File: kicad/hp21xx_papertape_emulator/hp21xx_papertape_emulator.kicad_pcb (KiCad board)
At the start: 2 copper layers, 66.5 x 61.2 mm, 85 parts, among them J1 SWD, J2 SERIAL, J3 Micro_SD_Card_Det_Hirose_DM3AT, J5 Conn_02x13_Odd_Even, SW1 Select, SW2 Up, SW3 Down, U1 TLV75533PDRV, U2 STM32F103C8Tx, U3 USBLC6-2SC6, U4 74HCT04, U5 74HCT245, U6 74LVC14, U7 74LVC245, Y1 8MHz

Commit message: New drivers.
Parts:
- removed U5: 74HCT245, Package_SO:TSSOP-20_4.4x6.5mm_P0.65mm
- added D7: 1N5819WS, Diode_SMD:D_SOD-323, F.Cu at (92.2, 113.0)
- added L1: 10uH, Inductor_SMD:L_0805_2012Metric, F.Cu at (96.1, 110.1)
- added Q1: 2N7002, Package_TO_SOT_SMD:SOT-23, F.Cu at (135.9, 87.8)
- added Q10: 2N7002, Package_TO_SOT_SMD:SOT-23, F.Cu at (114.2, 98.3)
- added Q11: 2N7002, Package_TO_SOT_SMD:SOT-23, F.Cu at (109.1, 98.3)
- added Q12: BSS84, Package_TO_SOT_SMD:SOT-23, F.Cu at (118.4, 106.0)
- added Q13: 2N7002, Package_TO_SOT_SMD:SOT-23, F.Cu at (132.1, 107.0)
- added Q14: 2N7002, Package_TO_SOT_SMD:SOT-23, F.Cu at (140.0, 105.8)
- added Q15: BSS84, Package_TO_SOT_SMD:SOT-23, F.Cu at (145.4, 105.6)
- added Q2: 2N7002, Package_TO_SOT_SMD:SOT-23, F.Cu at (144.7, 98.3)
- added Q3: 2N7002, Package_TO_SOT_SMD:SOT-23, F.Cu at (139.6, 98.3)
- added Q4: 2N7002, Package_TO_SOT_SMD:SOT-23, F.Cu at (143.2, 87.8)
- added Q5: 2N7002, Package_TO_SOT_SMD:SOT-23, F.Cu at (139.6, 87.8)
- added Q6: 2N7002, Package_TO_SOT_SMD:SOT-23, F.Cu at (134.5, 98.3)
- added Q7: 2N7002, Package_TO_SOT_SMD:SOT-23, F.Cu at (129.4, 98.3)
- added Q8: 2N7002, Package_TO_SOT_SMD:SOT-23, F.Cu at (124.3, 98.3)
- added Q9: 2N7002, Package_TO_SOT_SMD:SOT-23, F.Cu at (119.3, 98.3)
- added R100: 1k, Resistor_SMD:R_0402_1005Metric, F.Cu at (118.0, 96.3)
- added R101: 1k, Resistor_SMD:R_0402_1005Metric, F.Cu at (133.2, 96.3)
- added R102: 1k, Resistor_SMD:R_0402_1005Metric, F.Cu at (128.1, 96.3)
- added R103: 1k, Resistor_SMD:R_0402_1005Metric, F.Cu at (123.1, 96.3)
- added R104: 10k, Resistor_SMD:R_0402_1005Metric, F.Cu at (95.9, 115.3)
- added R19: 100k, Resistor_SMD:R_0402_1005Metric, F.Cu at (130.7, 96.3)
- added R45: 10k, Resistor_SMD:R_0402_1005Metric, F.Cu at (128.4, 101.5)
- added R46: 1k, Resistor_SMD:R_0402_1005Metric, F.Cu at (138.3, 96.3)
- added R54: 100, Resistor_SMD:R_0402_1005Metric, F.Cu at (136.8, 91.0)
- added R55: 100k, Resistor_SMD:R_0402_1005Metric, F.Cu at (137.1, 85.7)
- added R56: 10k, Resistor_SMD:R_0402_1005Metric, F.Cu at (134.8, 91.0)
- added R57: 100, Resistor_SMD:R_0402_1005Metric, F.Cu at (145.7, 101.5)
- added R58: 100k, Resistor_SMD:R_0402_1005Metric, F.Cu at (145.9, 96.3)
- added R59: 10k, Resistor_SMD:R_0402_1005Metric, F.Cu at (143.6, 101.5)
- added R60: 100, Resistor_SMD:R_0402_1005Metric, F.Cu at (140.6, 101.5)
- added R61: 100k, Resistor_SMD:R_0402_1005Metric, F.Cu at (140.8, 96.3)
- added R62: 10k, Resistor_SMD:R_0402_1005Metric, F.Cu at (138.6, 101.5)
- added R63: 100, Resistor_SMD:R_0402_1005Metric, F.Cu at (144.2, 91.0)
- added R64: 100k, Resistor_SMD:R_0402_1005Metric, F.Cu at (144.4, 85.6)
- added R65: 10k, Resistor_SMD:R_0402_1005Metric, F.Cu at (142.3, 91.0)
- added R66: 100, Resistor_SMD:R_0402_1005Metric, F.Cu at (140.5, 91.0)
- added R67: 100k, Resistor_SMD:R_0402_1005Metric, F.Cu at (140.8, 85.5)
- added R68: 10k, Resistor_SMD:R_0402_1005Metric, F.Cu at (138.5, 91.0)
- added R69: 100, Resistor_SMD:R_0402_1005Metric, F.Cu at (135.5, 101.5)
- added R70: 100k, Resistor_SMD:R_0402_1005Metric, F.Cu at (135.8, 96.3)
- added R71: 10k, Resistor_SMD:R_0402_1005Metric, F.Cu at (133.5, 101.5)
- added R72: 100, Resistor_SMD:R_0402_1005Metric, F.Cu at (125.3, 101.5)
- added R73: 100k, Resistor_SMD:R_0402_1005Metric, F.Cu at (125.6, 96.3)
- added R74: 10k, Resistor_SMD:R_0402_1005Metric, F.Cu at (123.3, 101.5)
- added R75: 100, Resistor_SMD:R_0402_1005Metric, F.Cu at (120.3, 101.5)
- added R76: 100k, Resistor_SMD:R_0402_1005Metric, F.Cu at (120.5, 96.3)
- added R77: 10k, Resistor_SMD:R_0402_1005Metric, F.Cu at (118.2, 101.5)
- added R78: 100, Resistor_SMD:R_0402_1005Metric, F.Cu at (115.2, 101.5)
- added R79: 100k, Resistor_SMD:R_0402_1005Metric, F.Cu at (115.4, 96.3)
- added R80: 10k, Resistor_SMD:R_0402_1005Metric, F.Cu at (113.2, 101.5)
- added R81: 100, Resistor_SMD:R_0402_1005Metric, F.Cu at (110.1, 101.5)
- added R82: 100k, Resistor_SMD:R_0402_1005Metric, F.Cu at (110.4, 96.3)
- added R83: 10k, Resistor_SMD:R_0402_1005Metric, F.Cu at (108.1, 101.5)
- added R84: 100, Resistor_SMD:R_0402_1005Metric, F.Cu at (119.4, 109.3)
- added R85: 100k, Resistor_SMD:R_0402_1005Metric, F.Cu at (131.1, 110.3)
- added R86: 100, Resistor_SMD:R_0402_1005Metric, F.Cu at (133.1, 110.3)
- added R87: 100k, Resistor_SMD:R_0402_1005Metric, F.Cu at (133.3, 104.9)
- added R88: 100, Resistor_SMD:R_0402_1005Metric, F.Cu at (129.8, 110.3)
- added R89: 100k, Resistor_SMD:R_0402_1005Metric, F.Cu at (144.5, 109.0)
- added R90: 100, Resistor_SMD:R_0402_1005Metric, F.Cu at (146.4, 109.0)
- added R91: 86.6k, Resistor_SMD:R_0402_1005Metric, F.Cu at (93.2, 115.3)
- added R93: 100k, Resistor_SMD:R_0402_1005Metric, F.Cu at (141.0, 109.2)
- added R94: 1k, Resistor_SMD:R_0402_1005Metric, F.Cu at (143.4, 96.3)
- added R95: 1k, Resistor_SMD:R_0402_1005Metric, F.Cu at (134.7, 85.6)
- added R96: 1k, Resistor_SMD:R_0402_1005Metric, F.Cu at (142.0, 85.6)
- added R97: 1k, Resistor_SMD:R_0402_1005Metric, F.Cu at (138.4, 85.7)
- added R98: 1k, Resistor_SMD:R_0402_1005Metric, F.Cu at (107.8, 96.3)
- added R99: 1k, Resistor_SMD:R_0402_1005Metric, F.Cu at (112.9, 96.3)
- C10, C11: value 100n -> 1u; footprint Capacitor_SMD:C_0402_1005Metric -> Capacitor_SMD:C_0805_2012Metric
- R10: value 100k -> 100
- U4: value 74HCT04 -> AP3012; footprint Package_SO:TSSOP-14_4.4x5mm_P0.65mm -> Package_TO_SOT_SMD:SOT-23-5
- moved C11 50.9 mm to (92.3, 109.0)
- moved U4 44.0 mm to (96.3, 113.0), turned to 0 degrees
- moved R10 28.7 mm to (130.4, 101.5)
- moved R3 16.8 mm to (102.9, 96.2)
- moved R4 16.5 mm to (95.2, 96.4)
- moved D1 16.4 mm to (99.9, 90.8)
- moved D2 16.4 mm to (92.6, 90.8)
- moved J5 16.4 mm to (106.7, 81.4)
- moved R11 16.4 mm to (109.2, 88.0)
- moved R23 16.4 mm to (124.5, 91.1)
- moved R27 16.4 mm to (121.9, 88.0)
- moved R35 16.4 mm to (127.0, 88.0)
- moved R37 16.4 mm to (129.5, 88.0)
- moved R41 16.4 mm to (132.2, 88.0)
- moved U6 16.4 mm to (148.8, 89.4)
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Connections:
- C11 pad 1: +5V -> +12V
- R10 pad 1: +5V -> /D3
- R10 pad 2: /RDREN -> Net-(Q7-G)
- U2 pad 20: unconnected-(U2-PB2-Pad20) -> /PUSEL
- U2 pad 46: /RDREN -> unconnected-(U2-PB9-Pad46)
- U4 pad 1: /FLAG_PTR -> Net-(D7-A)
- U4 pad 2: /OUTFR -> GND
- U4 pad 3: /PAPEROUT -> Net-(U4-FB)
- U4 pad 4: /PAPER_LOW -> /PUSEL
- U4 pad 5: /FLAG_PTP -> +5V
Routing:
- net /PU12V: track 0.00 -> 83.9 mm, vias 0 -> 13
- net /PU5V: track 0.00 -> 81.9 mm, vias 0 -> 14
- net +5V: track 155.1 -> 225.2 mm
- net /PUSEL: track 0.00 -> 60.0 mm, vias 0 -> 3
- net /D0: track 47.1 -> 106.6 mm, vias 3 -> 5
- net GND: track 105.5 -> 162.2 mm, vias 46 -> 74
- net /D1: track 45.5 -> 99.5 mm, vias 3 -> 5
- net +12V: track 0.00 -> 50.9 mm, vias 0 -> 5
- net /D2: track 44.2 -> 91.1 mm, vias 3 -> 5
- net /D3: track 42.1 -> 85.8 mm, vias 3 -> 5
- net +3.3V: track 46.7 -> 84.5 mm, vias 2 -> 4
- net /D4: track 40.6 -> 75.8 mm, vias 3 -> 5
- net /RDREN: track 34.0 -> 0.00 mm, vias 3 -> 0
- net /D5: track 37.5 -> 66.9 mm, vias 3 -> 5
- net /D7: track 36.6 -> 62.7 mm
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- added copper zone on F.Cu, net +3.3V
- added copper zone on B.Cu, net GND
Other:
- board size 66.5 x 61.2 mm -> 66.5 x 77.4 mm

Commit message: Fixed issues.
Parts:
- added C12: 4.7u, Capacitor_SMD:C_1206_3216Metric, F.Cu at (151.0, 95.7)
- added C13: 4.7u, Capacitor_SMD:C_1206_3216Metric, F.Cu at (148.7, 99.2)
- Q1, Q10, Q11, Q13, Q14, Q2, Q3, Q4, Q5, Q6, Q7, Q8, Q9: value 2N7002 -> BSS138
- moved R84 0.15 mm to (119.2, 109.4)
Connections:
- R84 pad 2: Net-(Q12-G) -> Net-(R84-Pad2)
- R90 pad 2: Net-(Q15-G) -> Net-(R90-Pad2)
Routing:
- net GND: track 162.2 -> 166.1 mm, vias 74 -> 75
- net Net-(Q12-G): track 1.91 -> 0.01 mm
- net Net-(U2-PB0): track 97.2 -> 95.9 mm
- net +5V: vias 14 -> 12
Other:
- board text added: "INCF"
- board text added: "INCP"
- board text added: "OUTFP"
- board text added: "OUTFR"
- board text added: "P_LOW"
- board text removed: "CMD"
- board text removed: "FLAG"

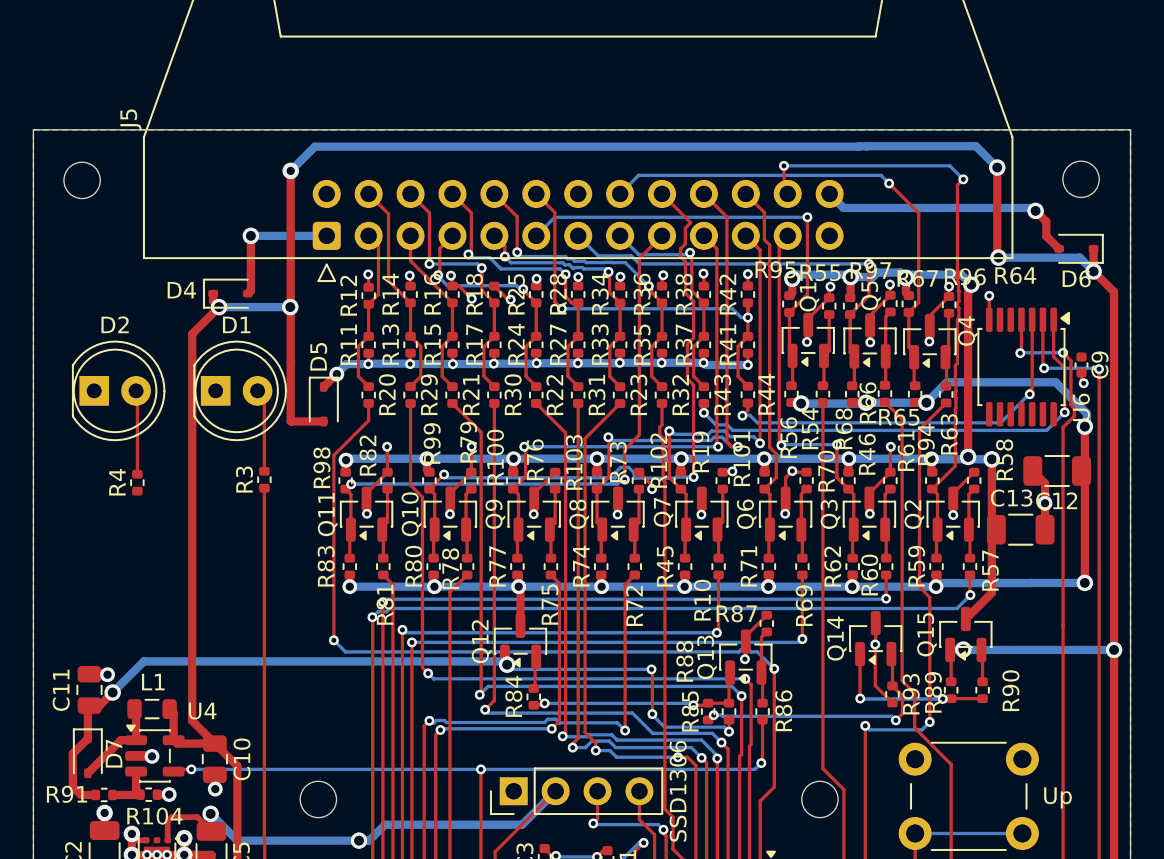
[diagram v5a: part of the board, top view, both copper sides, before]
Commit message: Fixed problems with net unconnected.
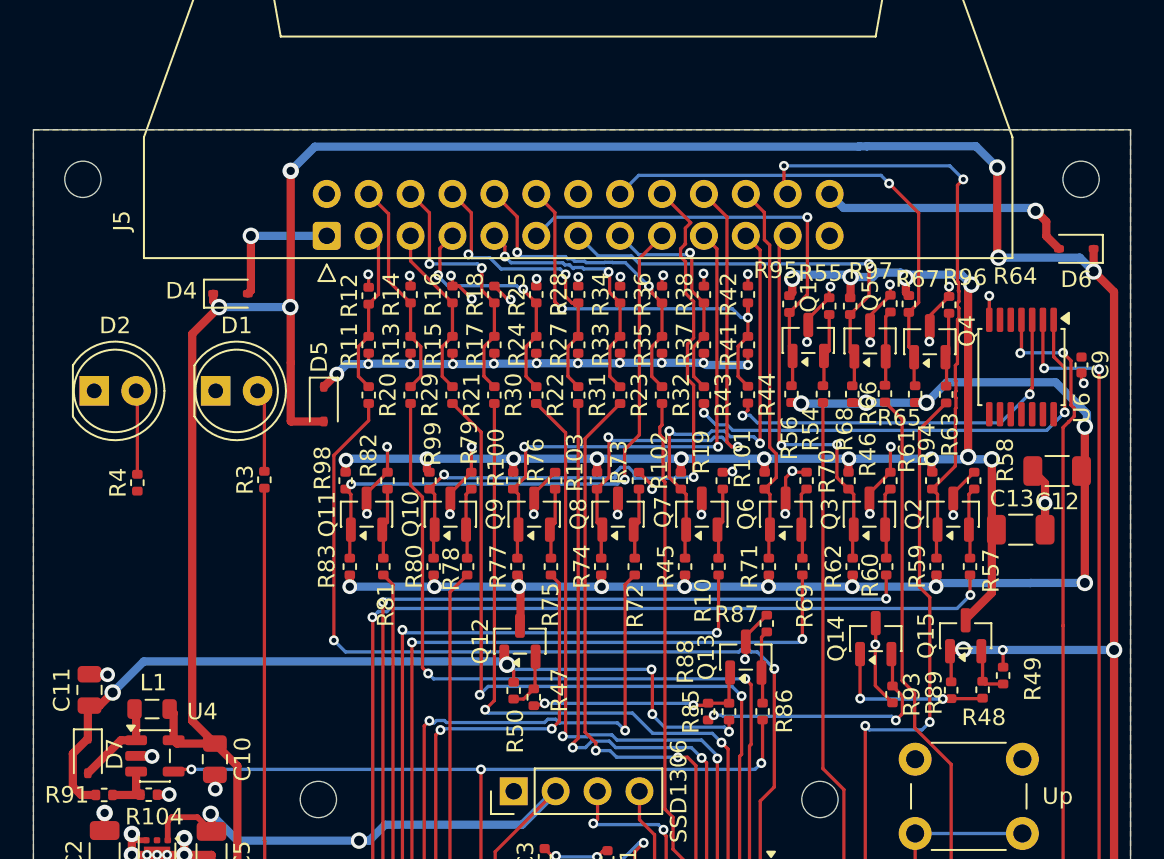
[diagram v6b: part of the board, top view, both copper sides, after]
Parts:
- removed R84, R90: 100, Resistor_SMD:R_0402_1005Metric
- added R47: 100, Resistor_SMD:R_0402_1005Metric, F.Cu at (119.2, 109.4)
- added R48: 100, Resistor_SMD:R_0402_1005Metric, F.Cu at (146.4, 108.9)
- added R49: 10k, Resistor_SMD:R_0402_1005Metric, F.Cu at (147.7, 108.1)
- added R50: 10k, Resistor_SMD:R_0402_1005Metric, F.Cu at (118.0, 109.0)
- moved Q15 0.08 mm to (145.4, 105.7)
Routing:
- net Net-(Q12-G): track 0.01 -> 1.48 mm
- net Net-(Q15-G): track 1.96 -> 3.27 mm
- net +12V: track 50.9 -> 52.1 mm
- net +5V: track 225.2 -> 226.2 mm, vias 12 -> 13

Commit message: spin 2
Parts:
- added D10: BAT54J, Diode_SMD:D_SOD-523, F.Cu at (159.7, 98.4)
- added D11: BAT54J, Diode_SMD:D_SOD-523, F.Cu at (159.7, 100.8)
- added D12: BAT54J, Diode_SMD:D_SOD-523, F.Cu at (159.7, 103.3)
- added D13: BAT54J, Diode_SMD:D_SOD-523, F.Cu at (159.7, 105.7)
- added D14: BAT54J, Diode_SMD:D_SOD-523, F.Cu at (163.3, 93.5)
- added D15: BAT54J, Diode_SMD:D_SOD-523, F.Cu at (163.3, 95.9)
- added D16: BAT54J, Diode_SMD:D_SOD-523, F.Cu at (138.3, 94.2)
- added D17: BAT54J, Diode_SMD:D_SOD-523, F.Cu at (138.6, 103.4)
- added D18: BAT54J, Diode_SMD:D_SOD-523, F.Cu at (163.3, 103.3)
- added D19: BAT54J, Diode_SMD:D_SOD-523, F.Cu at (163.3, 105.7)
- added D20: BAT54J, Diode_SMD:D_SOD-523, F.Cu at (166.9, 93.5)
- added D21: BAT54J, Diode_SMD:D_SOD-523, F.Cu at (166.9, 95.9)
- added D22: BAT54J, Diode_SMD:D_SOD-523, F.Cu at (166.9, 98.4)
- added D23: BAT54J, Diode_SMD:D_SOD-523, F.Cu at (166.9, 100.8)
- added D24: BAT54J, Diode_SMD:D_SOD-523, F.Cu at (166.9, 103.3)
- added D25: BAT54J, Diode_SMD:D_SOD-523, F.Cu at (166.9, 105.7)
- added D26: BAT54J, Diode_SMD:D_SOD-523, F.Cu at (170.5, 93.5)
- added D27: BAT54J, Diode_SMD:D_SOD-523, F.Cu at (170.5, 95.9)
- added D28: BAT54J, Diode_SMD:D_SOD-523, F.Cu at (170.5, 98.4)
- added D29: BAT54J, Diode_SMD:D_SOD-523, F.Cu at (170.5, 100.8)
- added D8: BAT54J, Diode_SMD:D_SOD-523, F.Cu at (159.7, 93.5)
- added D9: BAT54J, Diode_SMD:D_SOD-523, F.Cu at (159.7, 95.9)
- added R51: 10k, Resistor_SMD:R_0402_1005Metric, F.Cu at (173.7, 93.2)
- added R52: 10k, Resistor_SMD:R_0402_1005Metric, F.Cu at (173.7, 95.2)
- H2, H4, H6, H8: footprint MountingHole:MountingHole_2.2mm_M2 -> MountingHole:MountingHole_2.5mm
- L1: footprint Inductor_SMD:L_0805_2012Metric -> Inductor_SMD:L_Sunlord_SWPA3010S
- R1, R2: value 2k -> 10k
- R11, R13, R15, R17, R24, R27, R33, R35, R37, R41: footprint Resistor_SMD:R_0402_1005Metric -> Resistor_SMD:R_0805_2012Metric
- R87: value 100k -> 1k
- moved R89 3.79 mm to (148.2, 109.9)
- moved R93 1.92 mm to (139.1, 109.0)
- moved R48 1.92 mm to (144.5, 108.7)
- moved R47 1.80 mm to (117.5, 109.0)
- moved R49 1.40 mm to (146.4, 108.7)
- moved R50 1.38 mm to (119.4, 109.1)
- moved L1 0.85 mm to (96.0, 109.3)
- moved R62 0.26 mm to (138.6, 101.2)
- moved R83 0.25 mm to (108.1, 101.2)
- moved R46 0.12 mm to (138.3, 96.4)
- moved Q15 0.10 mm to (145.5, 105.7)
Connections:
- J3 pad 9: unconnected-(J3-DET_B-Pad9) -> GND
- Q1 pad 1: /OUTFP -> Net-(Q1-D)
- Q1 pad 2: Net-(Q1-G) -> GND
- Q1 pad 3: GND -> /OUTFP
- Q10 pad 1: /OUT6 -> Net-(Q10-D)
- Q10 pad 2: Net-(Q10-G) -> GND
- Q10 pad 3: GND -> /OUT6
- Q11 pad 1: /OUT7 -> Net-(Q11-G)
- Q11 pad 2: Net-(Q11-G) -> GND
- Q11 pad 3: GND -> /OUT7
- Q12 pad 1: +12V -> Net-(Q12-G)
- Q12 pad 2: Net-(Q12-G) -> +12V
- Q13 pad 1: Net-(Q13-D) -> Net-(Q13-G)
- Q13 pad 2: Net-(Q13-G) -> GND
- Q13 pad 3: GND -> Net-(Q13-D)
- Q14 pad 1: Net-(Q14-D) -> Net-(Q14-G)
- Q14 pad 2: Net-(Q14-G) -> GND
- Q14 pad 3: GND -> Net-(Q14-D)
- Q15 pad 1: +5V -> Net-(Q15-D)
- Q15 pad 2: Net-(Q15-G) -> +5V
- Q2 pad 1: /OUT0 -> Net-(Q2-D)
- Q2 pad 2: Net-(Q2-G) -> GND
- Q2 pad 3: GND -> /OUT0
- Q3 pad 1: /OUT1 -> Net-(Q3-D)
- Q3 pad 2: Net-(Q3-G) -> GND
- Q3 pad 3: GND -> /OUT1
- Q4 pad 1: /OUTFR -> Net-(Q4-D)
- Q4 pad 2: Net-(Q4-G) -> GND
- Q4 pad 3: GND -> /OUTFR
- Q5 pad 1: /PAPER_LOW -> Net-(Q5-G)
- Q5 pad 2: Net-(Q5-G) -> GND
- Q5 pad 3: GND -> /PAPER_LOW
- Q6 pad 1: /OUT2 -> Net-(Q6-D)
- Q6 pad 2: Net-(Q6-G) -> GND
- Q6 pad 3: GND -> /OUT2
- Q7 pad 1: /OUT3 -> Net-(Q7-D)
- Q7 pad 2: Net-(Q7-G) -> GND
- Q7 pad 3: GND -> /OUT3
- Q8 pad 1: /OUT4 -> Net-(Q8-D)
- Q8 pad 2: Net-(Q8-G) -> GND
- Q8 pad 3: GND -> /OUT4
- Q9 pad 1: /OUT5 -> Net-(Q9-D)
- Q9 pad 2: Net-(Q9-G) -> GND
- Q9 pad 3: GND -> /OUT5
- R10 pad 2: Net-(Q7-G) -> Net-(Q7-D)
- R100 pad 1: /PU5V -> Net-(D10-K)
- R101 pad 1: /PU5V -> Net-(D29-K)
- R102 pad 1: /PU5V -> Net-(D27-K)
- R103 pad 1: /PU5V -> Net-(D24-K)
- R19 pad 1: Net-(Q7-G) -> Net-(Q7-D)
- R45 pad 1: /PU12V -> Net-(D26-K)
- R46 pad 1: /PU5V -> Net-(D16-K)
- R48 pad 2: Net-(Q15-G) -> Net-(Q15-D)
- R49 pad 2: Net-(Q15-G) -> Net-(Q15-D)
- R54 pad 2: Net-(Q1-G) -> Net-(Q1-D)
- R55 pad 1: Net-(Q1-G) -> Net-(Q1-D)
- R56 pad 1: /PU12V -> Net-(D18-K)
- R57 pad 2: Net-(Q2-G) -> Net-(Q2-D)
- R58 pad 1: Net-(Q2-G) -> Net-(Q2-D)
- R59 pad 1: /PU12V -> Net-(D9-K)
- R60 pad 2: Net-(Q3-G) -> Net-(Q3-D)
- R61 pad 1: Net-(Q3-G) -> Net-(Q3-D)
- R62 pad 1: /PU12V -> Net-(D17-K)
- R63 pad 2: Net-(Q4-G) -> Net-(Q4-D)
- R64 pad 1: Net-(Q4-G) -> Net-(Q4-D)
- R65 pad 1: /PU12V -> Net-(D13-K)
- R68 pad 1: /PU12V -> Net-(D15-K)
- R69 pad 2: Net-(Q6-G) -> Net-(Q6-D)
- R70 pad 1: Net-(Q6-G) -> Net-(Q6-D)
- R71 pad 1: /PU12V -> Net-(D28-K)
- R72 pad 2: Net-(Q8-G) -> Net-(Q8-D)
- R73 pad 1: Net-(Q8-G) -> Net-(Q8-D)
- R74 pad 1: /PU12V -> Net-(D25-K)
- R75 pad 2: Net-(Q9-G) -> Net-(Q9-D)
- R76 pad 1: Net-(Q9-G) -> Net-(Q9-D)
- R77 pad 1: /PU12V -> Net-(D11-K)
- R78 pad 2: Net-(Q10-G) -> Net-(Q10-D)
- R79 pad 1: Net-(Q10-G) -> Net-(Q10-D)
- R80 pad 1: /PU12V -> Net-(D21-K)
- R83 pad 1: /PU12V -> Net-(D23-K)
- R94 pad 1: /PU5V -> Net-(D8-K)
- R95 pad 1: /PU5V -> Net-(D19-K)
- R96 pad 1: /PU5V -> Net-(D12-K)
- R97 pad 1: /PU5V -> Net-(D14-K)
- R98 pad 1: /PU5V -> Net-(D22-K)
- R99 pad 1: /PU5V -> Net-(D20-K)
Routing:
- net /PU12V: track 83.9 -> 31.1 mm, vias 13 -> 5
- net GND: track 166.1 -> 200.5 mm, vias 75 -> 72
- net /PAPEROUT: track 58.9 -> 36.7 mm
- net Net-(Q14-G): track 16.1 -> 1.06 mm, vias 2 -> 1
- net /PU5V: track 81.9 -> 68.7 mm, vias 14 -> 13
- net /FLAG_PTR: track 63.2 -> 51.4 mm, vias 4 -> 2
- net Net-(Q14-D): track 10.1 -> 0.00 mm, vias 2 -> 0
- net /OUT1: track 23.7 -> 18.4 mm
- net +5V: track 226.2 -> 220.9 mm, vias 13 -> 11
- net Net-(Q1-G): track 4.47 -> 0.00 mm
- net Net-(Q4-G): track 4.42 -> 0.00 mm
- net Net-(Q13-G): track 4.47 -> 0.09 mm
- net Net-(Q6-G): track 4.35 -> 0.00 mm
- net Net-(Q9-G): track 4.35 -> 0.00 mm
- net Net-(Q7-G): track 4.35 -> 0.00 mm
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- removed copper zone on F.Cu, net +3.3V
- removed copper zone on B.Cu, net GND
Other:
- board text added: "Note! This board only supports positive levels. I.e. the 12597A-01 / 12597-6002 board which uses ground and -12V as signal levels is NOT supported. Supported boards are: 12566A, 12566B and 12566C - Please check the jumpers for correct operation 12597A, 12597A-02 and 12597A-03 - Also check jumpers for correct operation"

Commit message: Fixed new spin.
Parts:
- added D30: BZX584B5V1, Diode_SMD:D_SOD-523, F.Cu at (132.9, 116.4)
- added D31: BZX584B5V1, Diode_SMD:D_SOD-523, F.Cu at (132.3, 113.7)
- added D32: BZX584B5V1, Diode_SMD:D_SOD-523, F.Cu at (131.5, 116.4)
- added D33: BZX584B5V1, Diode_SMD:D_SOD-523, F.Cu at (130.9, 113.7)
- added D34: BZX584B5V1, Diode_SMD:D_SOD-523, F.Cu at (130.1, 116.4)
- added D35: BZX584B5V1, Diode_SMD:D_SOD-523, F.Cu at (129.5, 113.7)
- added D36: BZX584B5V1, Diode_SMD:D_SOD-523, F.Cu at (128.7, 116.4)
- added D37: BZX584B5V1, Diode_SMD:D_SOD-523, F.Cu at (128.1, 113.7)
- added D38: BZX584B5V1, Diode_SMD:D_SOD-523, F.Cu at (150.7, 84.3)
- added D39: BZX584B5V1, Diode_SMD:D_SOD-523, F.Cu at (148.2, 84.3)
- moved D23 57.9 mm to (109.0, 103.5), turned to -90 degrees
- moved D22 56.9 mm to (110.2, 94.2), turned to 90 degrees
- moved D21 53.2 mm to (114.2, 103.4), turned to -90 degrees
- moved D20 51.6 mm to (115.3, 94.1), turned to 90 degrees
- moved D25 42.6 mm to (124.3, 103.3), turned to -90 degrees
- moved D24 42.4 mm to (125.4, 94.3), turned to 90 degrees
- moved D26 42.2 mm to (129.4, 103.4), turned to -90 degrees
- moved D11 40.5 mm to (119.3, 103.4), turned to -90 degrees
- moved D27 40.0 mm to (130.5, 94.2), turned to 90 degrees
- moved D10 39.5 mm to (120.4, 94.2), turned to 90 degrees
- moved D29 37.8 mm to (133.3, 94.2), turned to 90 degrees
- moved D28 36.3 mm to (134.5, 103.4), turned to -90 degrees
- moved D19 33.0 mm to (137.1, 85.5), turned to -90 degrees
- moved D18 29.3 mm to (135.9, 92.8), turned to -90 degrees
- moved R51 27.4 mm to (146.4, 95.9), turned to 180 degrees
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- renumbered R42 to Re
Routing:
- net /PU12V: track 31.1 -> 79.2 mm, vias 5 -> 14
- net /D0: track 106.6 -> 69.1 mm, vias 5 -> 3
- net GND: track 200.5 -> 163.6 mm, vias 72 -> 87
- net /PAPEROUT: track 36.7 -> 73.3 mm, vias 2 -> 4
- net /OUT1: track 18.4 -> 42.0 mm, vias 2 -> 4
- net Net-(Q13-D): track 14.1 -> 25.8 mm, vias 2 -> 4
- net Net-(Q14-D): track 0.00 -> 11.2 mm, vias 0 -> 2
- net Net-(D31-K): track 48.2 -> 58.5 mm, vias 2 -> 4
- net /FLAG_PTR: track 51.4 -> 60.1 mm
- net +3.3V: track 86.2 -> 94.1 mm, vias 4 -> 6
- net Net-(Q4-G): track 0.00 -> 5.50 mm, vias 0 -> 2
- net Net-(Q1-G): track 0.00 -> 4.82 mm, vias 0 -> 2
- net /OUT3: track 28.2 -> 23.8 mm, vias 3 -> 2
- net Net-(D36-K): track 35.7 -> 31.3 mm
- net Net-(Q15-G): track 0.09 -> 4.22 mm, vias 0 -> 2
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- added copper zone on F.Cu, net +3.3V
- added copper zone on B.Cu, net GND
